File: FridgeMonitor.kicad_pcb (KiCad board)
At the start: 2 copper layers, 78 x 62 mm, 277 parts, among them J1 Conn_01x03, J10 Conn_01x02_Pin, J11 Conn_01x03, J13 Conn_01x06_Pin, J2 Conn_01x03, J3 Conn_01x03, J4 Conn_01x03, J5 Conn_01x03, J6 Conn_02x04_Odd_Even, J7 USB_B_Micro, J8 Conn_01x02_Pin, J9 Conn_01x02_Pin, Q1 SI2301, U1 ESP-01v090, U2 LM2594M-3.3

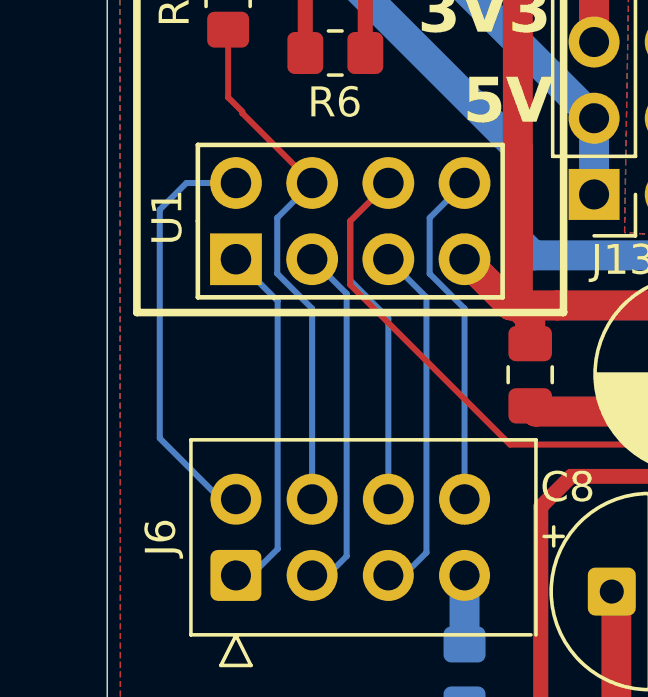
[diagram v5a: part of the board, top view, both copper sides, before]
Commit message: FIX: GND for ESP01 module
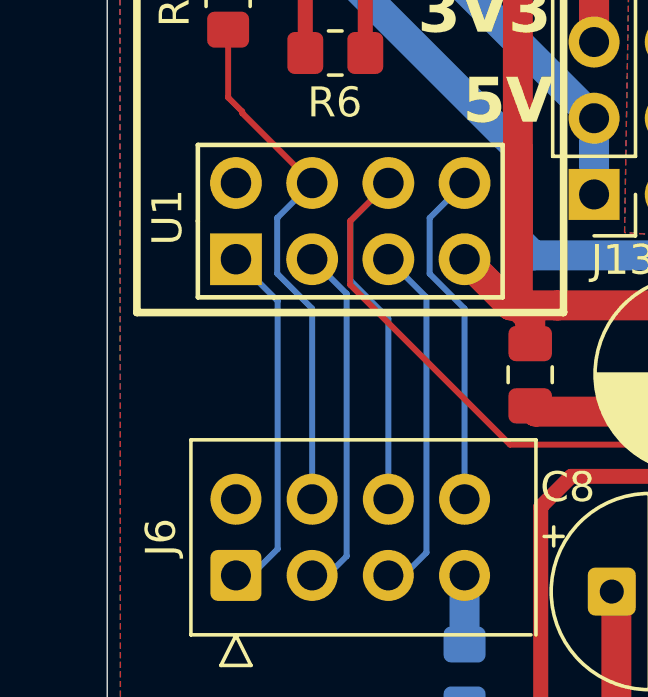
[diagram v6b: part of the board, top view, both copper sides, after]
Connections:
- J6 pad 2: Net-(J6-Pin_2) -> GND
- U1 pad 2: Net-(J6-Pin_2) -> GND
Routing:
- net Net-(J6-Pin_2): track 14.1 -> 0.00 mm
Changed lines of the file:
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@@
 			(layers "*.Cu" "*.Mask")
 			(remove_unused_layers no)
-			(net "Net-(J6-Pin_2)")
+			(net "GND")
 			(pinfunction "Pin_2_2")
 			(pintype "passive")
@@
 			(layers "*.Cu" "*.Mask" "F.SilkS")
 			(remove_unused_layers no)
-			(net "Net-(J6-Pin_2)")
+			(net "GND")
 			(pinfunction "GND_2")
 			(pintype "power_in")
@@
 	)
 	(segment
-		(start 32.639 63.881)
-		(end 34.29 63.881)
+		(start 35.68 67.811)
+		(end 34.29 66.421)
+		(width 0.2)
+		(layer "B.Cu")
+		(net "Net-(J6-Pin_1)")
+	)
+	(segment
+		(start 34.29 77.47)
+		(end 35.68 76.08)
+		(width 0.2)
+		(layer "B.Cu")
+		(net "Net-(J6-Pin_1)")
+	)
+	(segment
+		(start 35.68 76.08)
+		(end 35.68 67.811)
+		(width 0.2)
+		(layer "B.Cu")
+		(net "Net-(J6-Pin_1)")
+	)
+	(segment
+		(start 37.98 67.571)
+		(end 37.98 76.32)
+		(width 0.2)
+		(layer "B.Cu")
+		(net "Net-(J6-Pin_3)")
+	)
+	(segment
+		(start 36.83 66.421)
+		(end 37.98 67.571)
+		(width 0.2)
+		(layer "B.Cu")
+		(net "Net-(J6-Pin_3)")
+	)
+	(segment
+		(start 37.98 76.32)
+		(end 36.83 77.47)
+		(width 0.2)
+		(layer "B.Cu")
+		(net "Net-(J6-Pin_3)")
+	)
+	(segment
+		(start 34.5 61.5)
+		(end 34.029 61.029)
+		(width 0.2)
+		(layer "F.Cu")
+		(net "Net-(J6-Pin_4)")
+	)
+	(segment
+		(start 34.5 61.551)
+		(end 34.5 61.5)
+		(width 0.2)
+		(layer "F.Cu")
+		(net "Net-(J6-Pin_4)")
+	)
+	(segment
+		(start 34.029 61.029)
+		(end 34.029 58.77)
+		(width 0.2)
+		(layer "F.Cu")
+		(net "Net-(J6-Pin_4)")
+	)
+	(segment
+		(start 36.83 63.881)
+		(end 34.5 61.551)
+		(width 0.2)
+		(layer "F.Cu")
+		(net "Net-(J6-Pin_4)")
+	)
+	(segment
+		(start 35.6664 66.902979)
+		(end 35.6664 65.0446)
 		(width 0.2)
 		(layer "B.Cu")
-		(net "Net-(J6-Pin_2)")
+		(net "Net-(J6-Pin_4)")
 	)
 	(segment
-		(start 34.29 74.93)
-		(end 31.75 72.39)
+		(start 36.83 74.93)
+		(end 36.83 68.066579)
 		(width 0.2)
 		(layer "B.Cu")
-		(net "Net-(J6-Pin_2)")
+		(net "Net-(J6-Pin_4)")
 	)
 	(segment
-		(start 31.75 72.39)
-		(end 31.75 64.77)
+		(start 35.6664 65.0446)
+		(end 36.83 63.881)
 		(width 0.2)
 		(layer "B.Cu")
-		(net "Net-(J6-Pin_2)")
+		(net "Net-(J6-Pin_4)")
 	)
 	(segment
-		(start 31.75 64.77)
-		(end 32.639 63.881)
+		(start 36.83 68.066579)
+		(end 35.6664 66.902979)
 		(width 0.2)
 		(layer "B.Cu")
-		(net "Net-(J6-Pin_2)")
+		(net "Net-(J6-Pin_4)")
+	)
+	(segment
+		(start 39.37 66.421)
+		(end 40.64 67.691)
+		(width 0.2)
+		(layer "B.Cu")
+		(net "Net-(J6-Pin_5)")
+	)
+	(segment
+		(start 40.64 67.691)
+		(end 40.64 76.2)
+		(width 0.2)
+		(layer "B.Cu")
+		(net "Net-(J6-Pin_5)")
+	)
+	(segment
+		(start 40.64 76.2)
+		(end 39.37 77.47)
+		(width 0.2)
+		(layer "B.Cu")
+		(net "Net-(J6-Pin_5)")
+	)
+	(segment
+		(start 38.098 65.153)
+		(end 38.098 67.272)
+		(width 0.2)
+		(layer "F.Cu")
+		(net "Net-(J6-Pin_6)")
+	)
+	(segment
+		(start 39.37 63.881)
+		(end 38.098 65.153)
+		(width 0.2)
+		(layer "F.Cu")
+		(net "Net-(J6-Pin_6)")
+	)
+	(segment
+		(start 43.426 72.6)
+		(end 53.28 72.6)
+		(width 0.2)
+		(layer "F.Cu")
+		(net "Net-(J6-Pin_6)")
+	)
+	(segment
+		(start 53.28 72.6)
+		(end 54.61 73.93)
+		(width 0.2)
+		(layer "F.Cu")
+		(net "Net-(J6-Pin_6)")
+	)
+	(segment
+		(start 38.098 67.272)
+		(end 43.426 72.6)
+		(width 0.2)
+		(layer "F.Cu")
+		(net "Net-(J6-Pin_6)")
+	)
+	(segment
+		(start 38.1 65.151)
+		(end 39.37 63.881)
+		(width 0.2)
+		(layer "B.Cu")
+		(net "Net-(J6-Pin_6)")
+	)
+	(segment
+		(start 38.1 67.125314)
+		(end 38.1 65.151)
+		(width 0.2)
+		(layer "B.Cu")
+		(net "Net-(J6-Pin_6)")
+	)
+	(segment
+		(start 39.37 68.395314)
+		(end 38.1 67.125314)
+		(width 0.2)
+		(layer "B.Cu")
+		(net "Net-(J6-Pin_6)")
+	)
+	(segment
+		(start 39.37 74.93)
+		(end 39.37 68.395314)
+		(width 0.2)
+		(layer "B.Cu")
+		(net "Net-(J6-Pin_6)")
 	)
 	(segment
@@
 	)
 	(segment
+		(start 41.91 74.93)
+		(end 41.91 68.066579)
+		(width 0.2)
+		(layer "B.Cu")
+		(net "Net-(J6-Pin_8)")
+	)
+	(segment
+		(start 40.7464 65.0446)
+		(end 41.91 63.881)
+		(width 0.2)
+		(layer "B.Cu")
+		(net "Net-(J6-Pin_8)")
+	)
+	(segment
+		(start 41.91 68.066579)
+		(end 40.7464 66.902979)
+		(width 0.2)
+		(layer "B.Cu")
+		(net "Net-(J6-Pin_8)")
+	)
+	(segment
+		(start 40.7464 66.902979)
+		(end 40.7464 65.0446)
+		(width 0.2)
+		(layer "B.Cu")
+		(net "Net-(J6-Pin_8)")
+	)
+	(segment
 		(start 43.104 34.196)
 		(end 43.104 35.896)
@@
 		(net "Net-(D3-K)")
 	)
-	(segment
-		(start 41.91 74.93)
-		(end 41.91 68.066579)
-		(width 0.2)
-		(layer "B.Cu")
-		(net "Net-(J6-Pin_8)")
-	)
-	(segment
-		(start 40.7464 65.0446)
-		(end 41.91 63.881)
-		(width 0.2)
-		(layer "B.Cu")
-		(net "Net-(J6-Pin_8)")
-	)
-	(segment
-		(start 41.91 68.066579)
-		(end 40.7464 66.902979)
-		(width 0.2)
-		(layer "B.Cu")
-		(net "Net-(J6-Pin_8)")
-	)
-	(segment
-		(start 40.7464 66.902979)
-		(end 40.7464 65.0446)
-		(width 0.2)
-		(layer "B.Cu")
-		(net "Net-(J6-Pin_8)")
-	)
-	(segment
-		(start 35.68 67.811)
-		(end 34.29 66.421)
-		(width 0.2)
-		(layer "B.Cu")
-		(net "Net-(J6-Pin_1)")
-	)
-	(segment
-		(start 34.29 77.47)
-		(end 35.68 76.08)
-		(width 0.2)
-		(layer "B.Cu")
-		(net "Net-(J6-Pin_1)")
-	)
-	(segment
-		(start 35.68 76.08)
-		(end 35.68 67.811)
-		(width 0.2)
-		(layer "B.Cu")
-		(net "Net-(J6-Pin_1)")
-	)
-	(segment
-		(start 39.37 66.421)
-		(end 40.64 67.691)
-		(width 0.2)
-		(layer "B.Cu")
-		(net "Net-(J6-Pin_5)")
-	)
-	(segment
-		(start 40.64 67.691)
-		(end 40.64 76.2)
-		(width 0.2)
-		(layer "B.Cu")
-		(net "Net-(J6-Pin_5)")
-	)
-	(segment
-		(start 40.64 76.2)
-		(end 39.37 77.47)
-		(width 0.2)
-		(layer "B.Cu")
-		(net "Net-(J6-Pin_5)")
-	)
-	(segment
-		(start 37.98 67.571)
-		(end 37.98 76.32)
-		(width 0.2)
-		(layer "B.Cu")
-		(net "Net-(J6-Pin_3)")
-	)
-	(segment
-		(start 36.83 66.421)
-		(end 37.98 67.571)
-		(width 0.2)
-		(layer "B.Cu")
-		(net "Net-(J6-Pin_3)")
-	)
-	(segment
-		(start 37.98 76.32)
-		(end 36.83 77.47)
-		(width 0.2)
-		(layer "B.Cu")
-		(net "Net-(J6-Pin_3)")
-	)
-	(segment
-		(start 38.098 65.153)
-		(end 38.098 67.272)
-		(width 0.2)
-		(layer "F.Cu")
-		(net "Net-(J6-Pin_6)")
-	)
-	(segment
-		(start 39.37 63.881)
-		(end 38.098 65.153)
-		(width 0.2)
-		(layer "F.Cu")
-		(net "Net-(J6-Pin_6)")
-	)
-	(segment
-		(start 43.426 72.6)
-		(end 53.28 72.6)
-		(width 0.2)
-		(layer "F.Cu")
-		(net "Net-(J6-Pin_6)")
-	)
-	(segment
-		(start 53.28 72.6)
-		(end 54.61 73.93)
-		(width 0.2)
-		(layer "F.Cu")
-		(net "Net-(J6-Pin_6)")
-	)
-	(segment
-		(start 38.098 67.272)
-		(end 43.426 72.6)
-		(width 0.2)
-		(layer "F.Cu")
-		(net "Net-(J6-Pin_6)")
-	)
-	(segment
-		(start 38.1 65.151)
-		(end 39.37 63.881)
-		(width 0.2)
-		(layer "B.Cu")
-		(net "Net-(J6-Pin_6)")
-	)
-	(segment
-		(start 38.1 67.125314)
-		(end 38.1 65.151)
-		(width 0.2)
-		(layer "B.Cu")
-		(net "Net-(J6-Pin_6)")
-	)
-	(segment
-		(start 39.37 68.395314)
-		(end 38.1 67.125314)
-		(width 0.2)
-		(layer "B.Cu")
-		(net "Net-(J6-Pin_6)")
-	)
-	(segment
-		(start 39.37 74.93)
-		(end 39.37 68.395314)
-		(width 0.2)
-		(layer "B.Cu")
-		(net "Net-(J6-Pin_6)")
-	)
-	(segment
-		(start 34.5 61.5)
-		(end 34.029 61.029)
-		(width 0.2)
-		(layer "F.Cu")
-		(net "Net-(J6-Pin_4)")
-	)
-	(segment
-		(start 34.5 61.551)
-		(end 34.5 61.5)
-		(width 0.2)
-		(layer "F.Cu")
-		(net "Net-(J6-Pin_4)")
-	)
-	(segment
-		(start 34.029 61.029)
-		(end 34.029 58.77)
-		(width 0.2)
-		(layer "F.Cu")
-		(net "Net-(J6-Pin_4)")
-	)
-	(segment
-		(start 36.83 63.881)
-		(end 34.5 61.551)
-		(width 0.2)
-		(layer "F.Cu")
-		(net "Net-(J6-Pin_4)")
-	)
-	(segment
-		(start 35.6664 66.902979)
-		(end 35.6664 65.0446)
-		(width 0.2)
-		(layer "B.Cu")
-		(net "Net-(J6-Pin_4)")
-	)
-	(segment
-		(start 36.83 74.93)
-		(end 36.83 68.066579)
-		(width 0.2)
-		(layer "B.Cu")
-		(net "Net-(J6-Pin_4)")
-	)
-	(segment
-		(start 35.6664 65.0446)
-		(end 36.83 63.881)
-		(width 0.2)
-		(layer "B.Cu")
-		(net "Net-(J6-Pin_4)")
-	)
-	(segment
-		(start 36.83 68.066579)
-		(end 35.6664 66.902979)
-		(width 0.2)
-		(layer "B.Cu")
-		(net "Net-(J6-Pin_4)")
-	)
 	(zone
